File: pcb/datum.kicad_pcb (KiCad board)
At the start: 2 copper layers, 109 x 86.9 mm, 25 parts, among them J2 AudioJack4dpb, SW1 SW_Push, SW10 SW_Push, SW11 SW_Push, SW12 SW_Push, SW13 SW_Push, SW14 SW_Push, SW15 SW_Push, SW16 SW_Push, SW17 SW_Push, SW2 SW_Push, SW3 SW_Push, SW4 SW_Push, SW5 SW_Push, SW6 SW_Push, SW7 SW_Push, SW8 SW_Push, SW9 SW_Push, U1 ProMicro-kbd

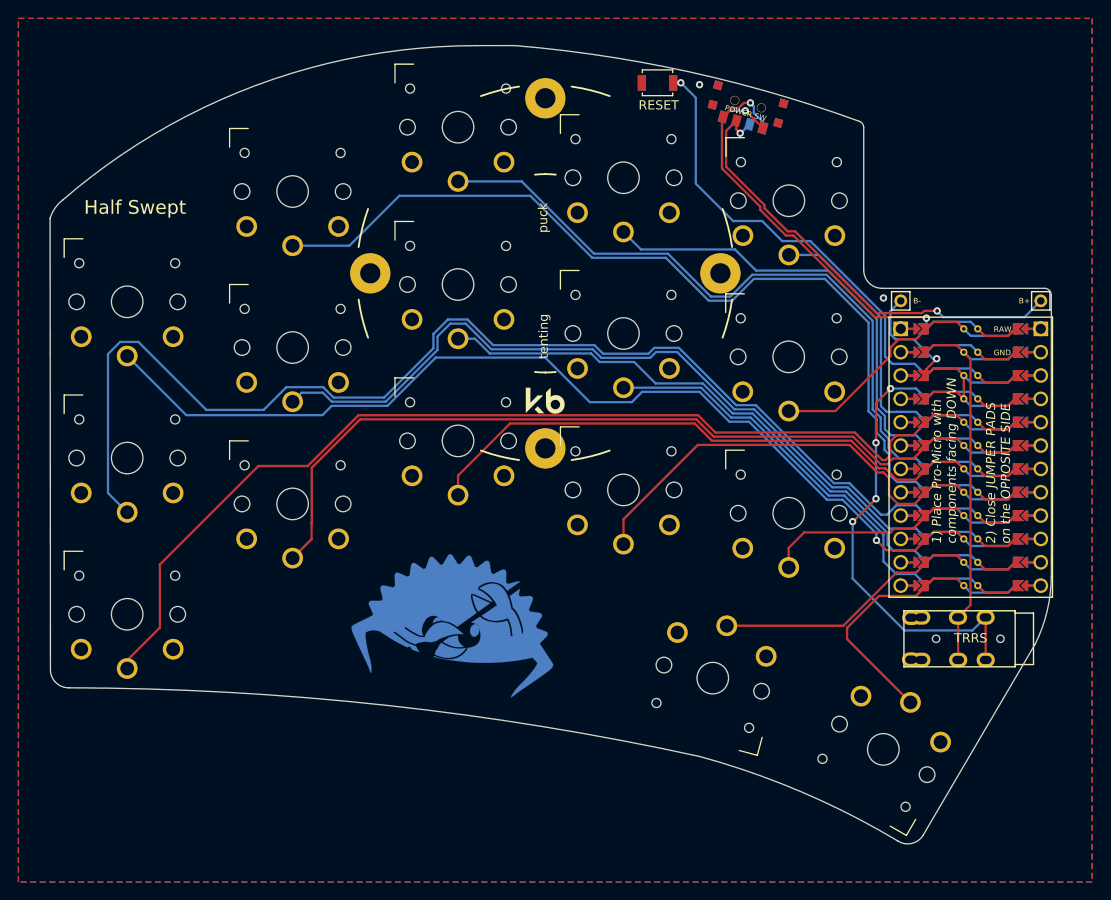
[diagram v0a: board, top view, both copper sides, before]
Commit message: cleanup: remove Sweep Half Swept branding and TRRS footprint
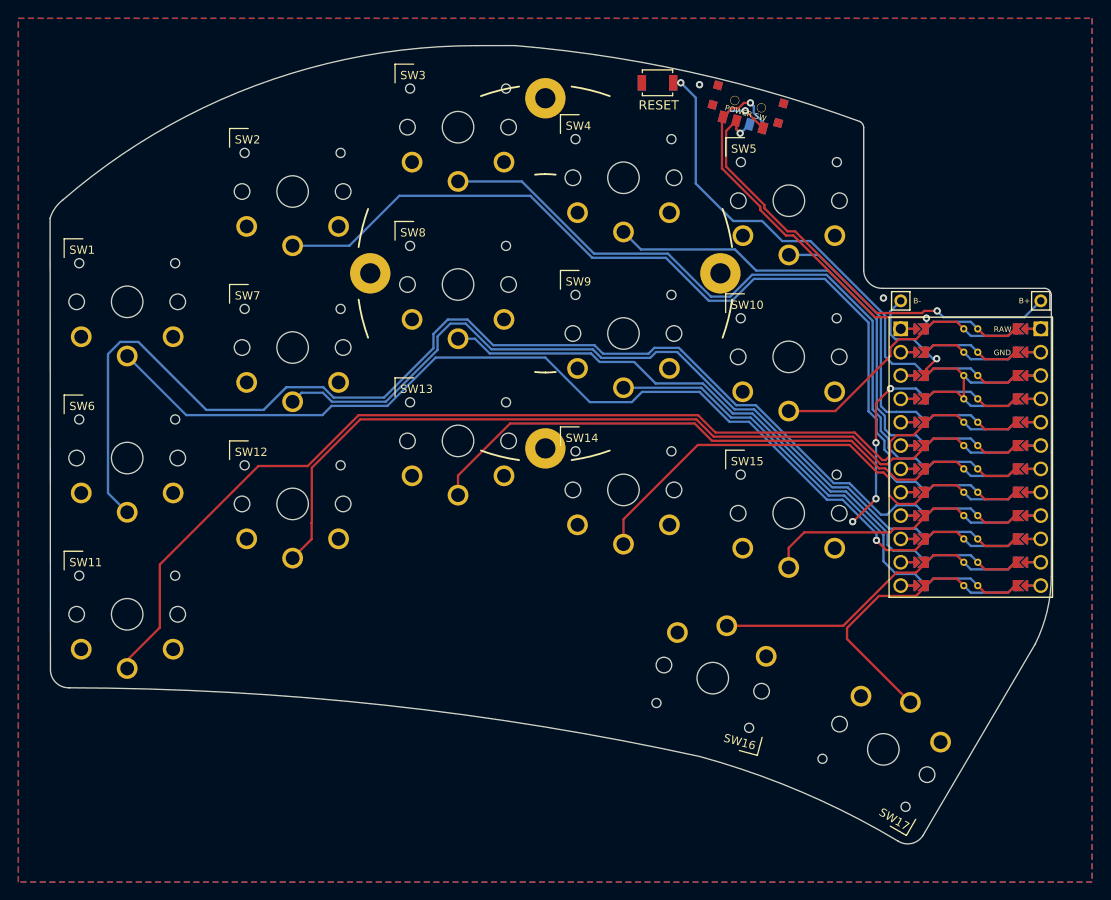
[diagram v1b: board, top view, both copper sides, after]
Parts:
- removed G***: LOGO, Kailh:ferris_broom
- removed J2: AudioJack4dpb, Kailh:TRRS-PJ-DPB2
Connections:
- RSW2 pad 1: gnd -> reset
- RSW2 pad 2: gnd -> reset
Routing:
- net Switch18: track 34.4 -> 0.00 mm
- net vcc: track 48.8 -> 20.6 mm
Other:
- board text removed: "1) Place Pro-Micro with components facing DOWN"
- board text removed: "2) Close JUMPER PADS on the OPPOSITE SIDE"
- board text removed: "Half Swept"
- board text removed: "TRRS"

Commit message: silkscreen: add datum branding and benchmark logo to both sides
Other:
- board text added: "Christian Faurholt"
- board text added: "datum"
- board text added: "made by"
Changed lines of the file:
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@@
+	)
+	(gr_line
+		(start 56.1 78.8)
+		(end 53.95 82.8)
+		(stroke
+			(width 0.2)
+			(type solid)
+		)
+		(layer "F.SilkS")
+	)
+	(gr_line
+		(start 56.1 78.8)
+		(end 56.1 82.8)
+		(stroke
+			(width 0.2)
+			(type solid)
+		)
+		(layer "F.SilkS")
+	)
+	(gr_line
+		(start 56.1 78.8)
+		(end 57.95 82.8)
+		(stroke
+			(width 0.2)
+			(type solid)
+		)
+		(layer "F.SilkS")
+	)
+	(gr_line
+		(start 57.95 78.6)
+		(end 53.95 78.6)
+		(stroke
+			(width 0.2)
+			(type solid)
+		)
+		(layer "F.SilkS")
+	)
+	(gr_line
+		(start 70.45 78.8)
+		(end 68.3 82.8)
+		(stroke
+			(width 0.2)
+			(type solid)
+		)
+		(layer "B.SilkS")
+	)
+	(gr_line
+		(start 70.45 78.8)
+		(end 70.45 82.8)
+		(stroke
+			(width 0.2)
+			(type solid)
+		)
+		(layer "B.SilkS")
+	)
+	(gr_line
+		(start 70.45 78.8)
+		(end 72.3 82.8)
+		(stroke
+			(width 0.2)
+			(type solid)
+		)
+		(layer "B.SilkS")
+	)
+	(gr_line
+		(start 72.3 78.6)
+		(end 68.3 78.6)
+		(stroke
+			(width 0.2)
+			(type solid)
+		)
+		(layer "B.SilkS")
 	)
 	(gr_line
@@
 		)
 	)
+	(gr_text "Christian Faurholt"
+		(at 58.55 83 0)
+		(layer "F.SilkS")
+		(effects
+			(font
+				(size 0.65 0.65)
+			)
+			(justify left bottom)
+		)
+	)
+	(gr_text "made by"
+		(at 58.55 82 0)
+		(layer "F.SilkS")
+		(effects
+			(font
+				(size 0.8 0.8)
+			)
+			(justify left bottom)
+		)
+	)
+	(gr_text "datum"
+		(at 58.35 81 0)
+		(layer "F.SilkS")
+		(effects
+			(font
+				(size 2 2)
+				(thickness 0.4)
+				(bold yes)
+			)
+			(justify left bottom)
+		)
+	)
 	(gr_text "RAW"
 		(at 116.40097 49.0728 0)
@@
 		)
 	)
+	(gr_text "Christian Faurholt"
+		(at 67.7 83 0)
+		(layer "B.SilkS")
+		(effects
+			(font
+				(size 0.65 0.65)
+			)
+			(justify left bottom mirror)
+		)
+	)
+	(gr_text "made by"
+		(at 67.7 82 0)
+		(layer "B.SilkS")
+		(effects
+			(font
+				(size 0.8 0.8)
+			)
+			(justify left bottom mirror)
+		)
+	)
+	(gr_text "datum"
+		(at 68 81 0)
+		(layer "B.SilkS")
+		(effects
+			(font
+				(size 2 2)
+				(thickness 0.4)
+				(bold yes)
+			)
+			(justify left bottom mirror)
+		)
+	)
